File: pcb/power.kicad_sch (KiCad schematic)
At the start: 10 parts, among them U5 AMS1117-5.0, U6 AMS1117-5.0

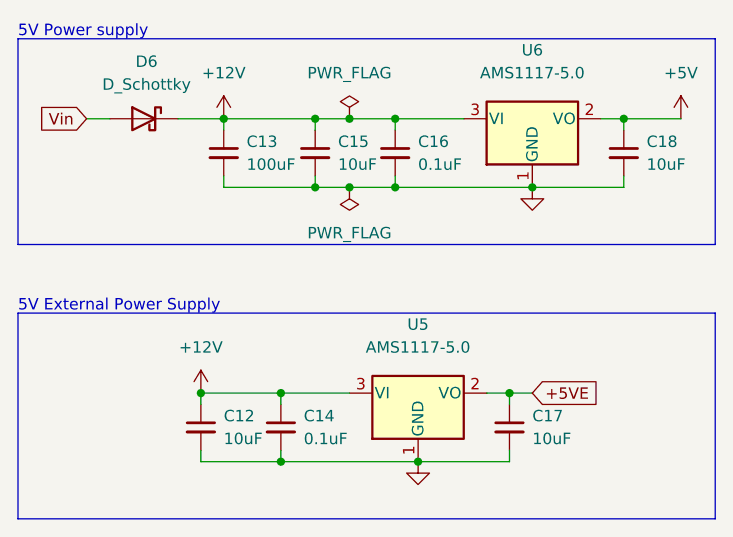
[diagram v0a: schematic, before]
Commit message: Fixed flyback/reverse polarity protection, added part #s
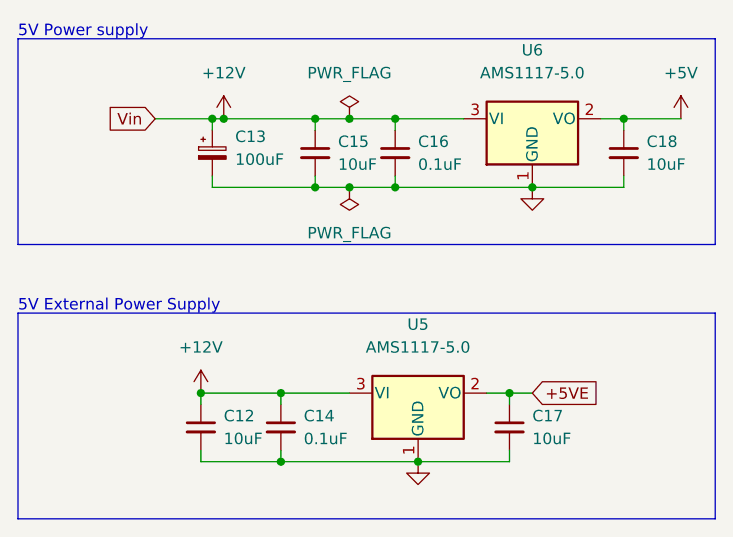
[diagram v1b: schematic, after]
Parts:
- removed C13: 100uF, Capacitor_SMD:C_1206_3216Metric, symbol Device:C_Small
- removed D6: D_Schottky, Diode_SMD:D_SOD-323, symbol Device:D_Schottky
- added C13: 100uF, Capacitor_SMD:C_Elec_6.3x7.7, symbol Device:C_Polarized_Small
- C12, C15, C17, C18: LCSC (none) -> C440198
- C14, C16: LCSC (none) -> C307331
- U5, U6: LCSC (none) -> C6187
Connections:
- net +12V: now also C13.1
- net GND: now also C13.2
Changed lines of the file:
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@@
   (junction (at 97.79 87.63) (diameter 0) (color 0 0 0 0)
   )
+  (junction (at 74.93 49.53) (diameter 0) (color 0 0 0 0)
+  )
   (junction (at 90.17 57.15) (diameter 0) (color 0 0 0 0)
   )
@@
     (stroke (width 0) (type default) (color 0 0 0 0))
   )
-  (wire (pts (xy 76.2 49.53) (xy 76.2 50.8))
+  (wire (pts (xy 74.93 49.53) (xy 74.93 50.8))
     (stroke (width 0) (type default) (color 0 0 0 0))
   )
@@
     (stroke (width 0) (type default) (color 0 0 0 0))
   )
+  (wire (pts (xy 74.93 49.53) (xy 76.2 49.53))
+    (stroke (width 0) (type default) (color 0 0 0 0))
+  )
   (wire (pts (xy 82.55 86.36) (xy 82.55 87.63))
     (stroke (width 0) (type default) (color 0 0 0 0))
@@
     (stroke (width 0) (type default) (color 0 0 0 0))
   )
-  (wire (pts (xy 76.2 55.88) (xy 76.2 57.15))
+  (wire (pts (xy 74.93 55.88) (xy 74.93 57.15))
     (stroke (width 0) (type default) (color 0 0 0 0))
   )
@@
     (stroke (width 0) (type default) (color 0 0 0 0))
   )
-  (wire (pts (xy 60.96 49.53) (xy 63.5 49.53))
-    (stroke (width 0) (type default) (color 0 0 0 0))
-  )
   (wire (pts (xy 90.17 49.53) (xy 86.36 49.53))
     (stroke (width 0) (type default) (color 0 0 0 0))
@@
     (stroke (width 0) (type default) (color 0 0 0 0))
   )
-  (wire (pts (xy 71.12 49.53) (xy 76.2 49.53))
+  (wire (pts (xy 68.58 49.53) (xy 74.93 49.53))
     (stroke (width 0) (type default) (color 0 0 0 0))
   )
@@
     (stroke (width 0) (type default) (color 0 0 0 0))
   )
-  (wire (pts (xy 76.2 57.15) (xy 86.36 57.15))
+  (wire (pts (xy 74.93 57.15) (xy 86.36 57.15))
     (stroke (width 0) (type default) (color 0 0 0 0))
   )
@@
     )
   )
-  (global_label "Vin" (shape input) (at 60.96 49.53 180) (fields_autoplaced)
+  (global_label "Vin" (shape input) (at 68.58 49.53 180) (fields_autoplaced)
     (effects (font (size 1.27 1.27)) (justify right))
-    (property "Intersheet References" "${INTERSHEET_REFS}" (id 0) (at 55.7045 49.6094 0)
+    (property "Intersheet References" "${INTERSHEET_REFS}" (id 0) (at 63.3245 49.6094 0)
       (effects (font (size 1.27 1.27)) (justify right) hide)
     )
@@
       (effects (font (size 1.27 1.27)) hide)
     )
+    (property "LCSC" "C440198" (id 7) (at 107.95 83.82 0)
+      (effects (font (size 1.27 1.27)) hide)
+    )
     (pin "1")
     (pin "2")
@@
       (effects (font (size 1.27 1.27)) hide)
     )
+    (property "LCSC" "C440198" (id 7) (at 120.65 53.34 0)
+      (effects (font (size 1.27 1.27)) hide)
+    )
     (pin "1")
     (pin "2")
@@
       (effects (font (size 1.27 1.27)) hide)
     )
+    (property "LCSC" "C6187" (id 4) (at 97.79 80.01 0)
+      (effects (font (size 1.27 1.27)) hide)
+    )
     (pin "1")
     (pin "2")
     (pin "3")
   )
-  (symbol (lib_id "Device:C_Small") (at 76.2 53.34 0) (unit 1)
-    (in_bom yes) (on_board yes) (fields_autoplaced)
-    (property "Reference" "C13" (id 0) (at 78.74 52.0762 0)
-      (effects (font (size 1.27 1.27)) (justify left))
-    )
-    (property "Value" "100uF" (id 1) (at 78.74 54.6162 0)
-      (effects (font (size 1.27 1.27)) (justify left))
-    )
-    (property "Footprint" "Capacitor_SMD:C_1206_3216Metric" (id 2) (at 76.2 53.34 0)
-      (effects (font (size 1.27 1.27)) hide)
-    )
-    (property "Datasheet" "~" (id 3) (at 76.2 53.34 0)
-      (effects (font (size 1.27 1.27)) hide)
-    )
-    (property "Spice_Primitive" "C" (id 4) (at 76.2 53.34 0)
-      (effects (font (size 1.27 1.27)) hide)
-    )
-    (property "Spice_Model" "100u" (id 5) (at 76.2 53.34 0)
-      (effects (font (size 1.27 1.27)) hide)
-    )
-    (property "Spice_Netlist_Enabled" "N" (id 6) (at 76.2 53.34 0)
-      (effects (font (size 1.27 1.27)) hide)
-    )
-    (pin "1")
-    (pin "2")
-  )
   (symbol (lib_id "Device:C_Small") (at 95.25 53.34 0) (unit 1)
     (in_bom yes) (on_board yes) (fields_autoplaced)
@@
       (effects (font (size 1.27 1.27)) hide)
     )
-    (pin "1")
-    (pin "2")
-  )
-  (symbol (lib_id "Device:D_Schottky") (at 67.31 49.53 0) (mirror y) (unit 1)
-    (in_bom yes) (on_board yes) (fields_autoplaced)
-    (property "Reference" "D6" (id 0) (at 67.6275 43.18 0))
-    (property "Value" "D_Schottky" (id 1) (at 67.6275 45.72 0))
-    (property "Footprint" "Diode_SMD:D_SOD-323" (id 2) (at 67.31 49.53 0)
-      (effects (font (size 1.27 1.27)) hide)
-    )
-    (property "Datasheet" "~" (id 3) (at 67.31 49.53 0)
-      (effects (font (size 1.27 1.27)) hide)
-    )
-    (property "Spice_Primitive" "D" (id 4) (at 67.31 49.53 0)
-      (effects (font (size 1.27 1.27)) hide)
-    )
-    (property "Spice_Model" "D_Schottky" (id 5) (at 67.31 49.53 0)
-      (effects (font (size 1.27 1.27)) hide)
-    )
-    (property "Spice_Netlist_Enabled" "N" (id 6) (at 67.31 49.53 0)
+    (property "LCSC" "C307331" (id 7) (at 95.25 53.34 0)
       (effects (font (size 1.27 1.27)) hide)
     )
@@
       (effects (font (size 1.27 1.27)) hide)
     )
+    (property "LCSC" "C440198" (id 7) (at 73.66 83.82 0)
+      (effects (font (size 1.27 1.27)) hide)
+    )
     (pin "1")
     (pin "2")
@@
       (effects (font (size 1.27 1.27)) hide)
     )
+    (property "LCSC" "C440198" (id 7) (at 86.36 53.34 0)
+      (effects (font (size 1.27 1.27)) hide)
+    )
     (pin "1")
     (pin "2")
@@
     )
     (property "Spice_Netlist_Enabled" "N" (id 6) (at 82.55 83.82 0)
+      (effects (font (size 1.27 1.27)) hide)
+    )
+    (property "LCSC" "C307331" (id 7) (at 82.55 83.82 0)
+      (effects (font (size 1.27 1.27)) hide)
+    )
+    (pin "1")
+    (pin "2")
+  )
+  (symbol (lib_id "Device:C_Polarized_Small") (at 74.93 53.34 0) (unit 1)
+    (in_bom yes) (on_board yes)
+    (property "Reference" "C13" (id 0) (at 77.47 51.5238 0)
+      (effects (font (size 1.27 1.27)) (justify left))
+    )
+    (property "Value" "100uF" (id 1) (at 77.47 54.0638 0)
+      (effects (font (size 1.27 1.27)) (justify left))
+    )
+    (property "Footprint" "Capacitor_SMD:C_Elec_6.3x7.7" (id 2) (at 74.93 53.34 0)
+      (effects (font (size 1.27 1.27)) hide)
+    )
+    (property "Datasheet" "~" (id 3) (at 74.93 53.34 0)
+      (effects (font (size 1.27 1.27)) hide)
+    )
+    (property "LCSC" "C2836437" (id 4) (at 74.93 53.34 0)
       (effects (font (size 1.27 1.27)) hide)
     )
@@
       (effects (font (size 1.27 1.27)) hide)
     )
+    (property "LCSC" "C6187" (id 4) (at 110.49 49.53 0)
+      (effects (font (size 1.27 1.27)) hide)
+    )

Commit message: Switch to M12 Connector, fix comparator issue from rev 5
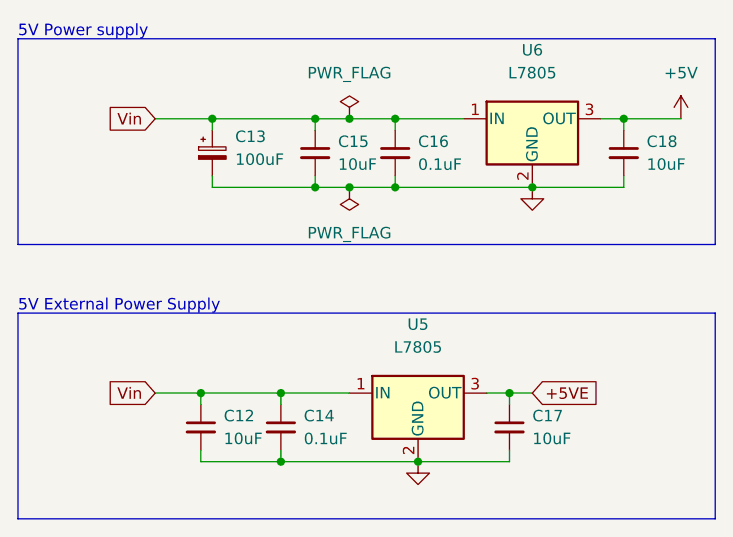
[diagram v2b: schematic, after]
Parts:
- removed U5, U6: AMS1117-5.0, Package_TO_SOT_SMD:SOT-223-3_TabPin2, symbol Regulator_Linear:AMS1117-5.0
- added U5, U6: L7805, Package_TO_SOT_SMD:TO-252-2, symbol Regulator_Linear:L7805
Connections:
- net +5V: now also U6.3 (OUT)
- net +5VE: now also U5.3 (OUT)
- net GND: now also U5.2 (GND), U6.2 (GND)
- net +12V renamed Vin
- net Vin: now also U5.1 (IN), U6.1 (IN)
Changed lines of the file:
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@@
   (junction (at 82.55 80.01) (diameter 0) (color 0 0 0 0)
   )
+  (junction (at 90.17 49.53) (diameter 0) (color 0 0 0 0)
+  )
+  (junction (at 82.55 87.63) (diameter 0) (color 0 0 0 0)
+  )
+  (junction (at 95.25 49.53) (diameter 0) (color 0 0 0 0)
+  )
+  (junction (at 110.49 57.15) (diameter 0) (color 0 0 0 0)
+  )
+  (junction (at 97.79 87.63) (diameter 0) (color 0 0 0 0)
+  )
   (junction (at 73.66 80.01) (diameter 0) (color 0 0 0 0)
   )
-  (junction (at 90.17 49.53) (diameter 0) (color 0 0 0 0)
-  )
-  (junction (at 82.55 87.63) (diameter 0) (color 0 0 0 0)
-  )
-  (junction (at 95.25 49.53) (diameter 0) (color 0 0 0 0)
-  )
-  (junction (at 110.49 57.15) (diameter 0) (color 0 0 0 0)
-  )
-  (junction (at 97.79 87.63) (diameter 0) (color 0 0 0 0)
-  )
   (junction (at 74.93 49.53) (diameter 0) (color 0 0 0 0)
   )
@@
   (junction (at 86.36 49.53) (diameter 0) (color 0 0 0 0)
   )
-  (junction (at 76.2 49.53) (diameter 0) (color 0 0 0 0)
-  )
   (junction (at 95.25 57.15) (diameter 0) (color 0 0 0 0)
   )
@@
     (stroke (width 0) (type default) (color 0 0 0 0))
   )
-  (wire (pts (xy 76.2 49.53) (xy 86.36 49.53))
+  (wire (pts (xy 74.93 49.53) (xy 86.36 49.53))
     (stroke (width 0) (type default) (color 0 0 0 0))
   )
@@
     (stroke (width 0) (type default) (color 0 0 0 0))
   )
+  (wire (pts (xy 68.58 80.01) (xy 73.66 80.01))
+    (stroke (width 0) (type default) (color 0 0 0 0))
+  )
   (wire (pts (xy 82.55 87.63) (xy 97.79 87.63))
     (stroke (width 0) (type default) (color 0 0 0 0))
@@
   )
   (wire (pts (xy 118.11 49.53) (xy 120.65 49.53))
-    (stroke (width 0) (type default) (color 0 0 0 0))
-  )
-  (wire (pts (xy 74.93 49.53) (xy 76.2 49.53))
     (stroke (width 0) (type default) (color 0 0 0 0))
   )
@@
   (text "5V Power supply" (at 53.34 40.64 0)
     (effects (font (size 1.27 1.27)) (justify left bottom))
+  )
+  (global_label "Vin" (shape input) (at 68.58 49.53 180) (fields_autoplaced)
+    (effects (font (size 1.27 1.27)) (justify right))
+    (property "Intersheet References" "${INTERSHEET_REFS}" (id 0) (at 63.3245 49.6094 0)
+      (effects (font (size 1.27 1.27)) (justify right) hide)
+    )
   )
   (global_label "+5VE" (shape input) (at 110.49 80.01 0) (fields_autoplaced)
@@
     )
   )
-  (global_label "Vin" (shape input) (at 68.58 49.53 180) (fields_autoplaced)
+  (global_label "Vin" (shape input) (at 68.58 80.01 180) (fields_autoplaced)
     (effects (font (size 1.27 1.27)) (justify right))
-    (property "Intersheet References" "${INTERSHEET_REFS}" (id 0) (at 63.3245 49.6094 0)
+    (property "Intersheet References" "${INTERSHEET_REFS}" (id 0) (at 63.3245 80.0894 0)
       (effects (font (size 1.27 1.27)) (justify right) hide)
     )
@@
     (pin "1")
   )
-  (symbol (lib_id "power:+12V") (at 76.2 49.53 0) (unit 1)
-    (in_bom yes) (on_board yes) (fields_autoplaced)
-    (property "Reference" "#PWR056" (id 0) (at 76.2 53.34 0)
-      (effects (font (size 1.27 1.27)) hide)
-    )
-    (property "Value" "+12V" (id 1) (at 76.2 44.45 0))
-    (property "Footprint" "" (id 2) (at 76.2 49.53 0)
-      (effects (font (size 1.27 1.27)) hide)
-    )
-    (property "Datasheet" "" (id 3) (at 76.2 49.53 0)
-      (effects (font (size 1.27 1.27)) hide)
-    )
-    (pin "1")
-  )
   (symbol (lib_id "power:+5V") (at 127 49.53 0) (unit 1)
     (in_bom yes) (on_board yes) (fields_autoplaced)
-    (property "Reference" "#PWR059" (id 0) (at 127 53.34 0)
+    (property "Reference" "#PWR042" (id 0) (at 127 53.34 0)
       (effects (font (size 1.27 1.27)) hide)
     )
@@
     )
     (pin "1")
+  )
+  (symbol (lib_id "Regulator_Linear:L7805") (at 110.49 49.53 0) (unit 1)
+    (in_bom yes) (on_board yes) (fields_autoplaced)
+    (property "Reference" "U6" (id 0) (at 110.49 41.91 0))
+    (property "Value" "L7805" (id 1) (at 110.49 44.45 0))
+    (property "Footprint" "Package_TO_SOT_SMD:TO-252-2" (id 2) (at 111.125 53.34 0)
+      (effects (font (size 1.27 1.27) italic) (justify left) hide)
+    )
+    (property "Datasheet" "http://www.st.com/content/ccc/resource/technical/document/datasheet/41/4f/b3/b0/12/d4/47/88/CD00000444.pdf/files/CD00000444.pdf/jcr:content/translations/en.CD00000444.pdf" (id 3) (at 110.49 50.8 0)
+      (effects (font (size 1.27 1.27)) hide)
+    )
+    (pin "1")
+    (pin "2")
+    (pin "3")
   )
   (symbol (lib_id "Device:C_Small") (at 107.95 83.82 0) (unit 1)
@@
     (pin "2")
   )
-  (symbol (lib_id "Regulator_Linear:AMS1117-5.0") (at 97.79 80.01 0) (unit 1)
-    (in_bom yes) (on_board yes) (fields_autoplaced)
-    (property "Reference" "U5" (id 0) (at 97.79 72.39 0))
-    (property "Value" "AMS1117-5.0" (id 1) (at 97.79 74.93 0))
-    (property "Footprint" "Package_TO_SOT_SMD:SOT-223-3_TabPin2" (id 2) (at 97.79 74.93 0)
-      (effects (font (size 1.27 1.27)) hide)
-    )
-    (property "Datasheet" "http://www.advanced-monolithic.com/pdf/ds1117.pdf" (id 3) (at 100.33 86.36 0)
-      (effects (font (size 1.27 1.27)) hide)
-    )
-    (property "LCSC" "C6187" (id 4) (at 97.79 80.01 0)
-      (effects (font (size 1.27 1.27)) hide)
-    )
-    (pin "1")
-    (pin "2")
-    (pin "3")
-  )
   (symbol (lib_id "Device:C_Small") (at 95.25 53.34 0) (unit 1)
     (in_bom yes) (on_board yes) (fields_autoplaced)
@@
     (pin "2")
   )
+  (symbol (lib_id "Regulator_Linear:L7805") (at 97.79 80.01 0) (unit 1)
+    (in_bom yes) (on_board yes) (fields_autoplaced)
+    (property "Reference" "U5" (id 0) (at 97.79 72.39 0))
+    (property "Value" "L7805" (id 1) (at 97.79 74.93 0))
+    (property "Footprint" "Package_TO_SOT_SMD:TO-252-2" (id 2) (at 98.425 83.82 0)
+      (effects (font (size 1.27 1.27) italic) (justify left) hide)
+    )
+    (property "Datasheet" "http://www.st.com/content/ccc/resource/technical/document/datasheet/41/4f/b3/b0/12/d4/47/88/CD00000444.pdf/files/CD00000444.pdf/jcr:content/translations/en.CD00000444.pdf" (id 3) (at 97.79 81.28 0)
+      (effects (font (size 1.27 1.27)) hide)
+    )
+    (pin "1")
+    (pin "2")
+    (pin "3")
+  )
   (symbol (lib_id "power:PWR_FLAG") (at 90.17 57.15 180) (unit 1)
     (in_bom yes) (on_board yes) (fields_autoplaced)
@@
     (pin "2")
   )
-  (symbol (lib_id "power:+12V") (at 73.66 80.01 0) (unit 1)
-    (in_bom yes) (on_board yes) (fields_autoplaced)
-    (property "Reference" "#PWR055" (id 0) (at 73.66 83.82 0)
-      (effects (font (size 1.27 1.27)) hide)
-    )
-    (property "Value" "+12V" (id 1) (at 73.66 74.93 0))
-    (property "Footprint" "" (id 2) (at 73.66 80.01 0)
-      (effects (font (size 1.27 1.27)) hide)
-    )
-    (property "Datasheet" "" (id 3) (at 73.66 80.01 0)
-      (effects (font (size 1.27 1.27)) hide)
-    )
-    (pin "1")
-  )
   (symbol (lib_id "power:GND") (at 97.79 87.63 0) (unit 1)
     (in_bom yes) (on_board yes) (fields_autoplaced)
-    (property "Reference" "#PWR057" (id 0) (at 97.79 93.98 0)
+    (property "Reference" "#PWR040" (id 0) (at 97.79 93.98 0)
       (effects (font (size 1.27 1.27)) hide)
     )
@@
   (symbol (lib_id "power:GND") (at 110.49 57.15 0) (unit 1)
     (in_bom yes) (on_board yes) (fields_autoplaced)
-    (property "Reference" "#PWR058" (id 0) (at 110.49 63.5 0)
+    (property "Reference" "#PWR041" (id 0) (at 110.49 63.5 0)
       (effects (font (size 1.27 1.27)) hide)
     )
@@
     (pin "2")
   )
-  (symbol (lib_id "Regulator_Linear:AMS1117-5.0") (at 110.49 49.53 0) (unit 1)
-    (in_bom yes) (on_board yes) (fields_autoplaced)
-    (property "Reference" "U6" (id 0) (at 110.49 41.91 0))
-    (property "Value" "AMS1117-5.0" (id 1) (at 110.49 44.45 0))
-    (property "Footprint" "Package_TO_SOT_SMD:SOT-223-3_TabPin2" (id 2) (at 110.49 44.45 0)
-      (effects (font (size 1.27 1.27)) hide)
-    )
-    (property "Datasheet" "http://www.advanced-monolithic.com/pdf/ds1117.pdf" (id 3) (at 113.03 55.88 0)
-      (effects (font (size 1.27 1.27)) hide)
-    )
-    (property "LCSC" "C6187" (id 4) (at 110.49 49.53 0)
-      (effects (font (size 1.27 1.27)) hide)
-    )
-    (pin "1")
-    (pin "2")
-    (pin "3")
-  )
 )

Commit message: Added jlc part number for 7805
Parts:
- U5, U6: LCSC (none) -> C897464
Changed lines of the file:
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@@
+      (effects (font (size 1.27 1.27)) hide)
+    )
+    (property "LCSC" "C897464" (id 4) (at 110.49 49.53 0)
       (effects (font (size 1.27 1.27)) hide)
     )
@@
       (effects (font (size 1.27 1.27)) hide)
     )
+    (property "LCSC" "C897464" (id 4) (at 97.79 80.01 0)
+      (effects (font (size 1.27 1.27)) hide)
+    )

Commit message: Update to KiCad 7, bump project revision/date
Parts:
- C12, C15, C17, C18: Spice_Model 10u -> (none); Spice_Netlist_Enabled N -> (none); Spice_Primitive C -> (none)
- C14, C16: Spice_Model 0.1u -> (none); Spice_Netlist_Enabled N -> (none); Spice_Primitive C -> (none)
